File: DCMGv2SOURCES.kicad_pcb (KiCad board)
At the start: 2 copper layers, 232.7 x 74.2 mm, 170 parts, among them P10 NC_SCGR_SIG, P14 UNREG_V_SIG, P15 UNREG_I_SIG, P16 TO_REG+, P17 TO_REG-, P18 FROM_REG+, P19 FROM_REG-, P20 REG_V_SIG, P21 TO_GRID-, P22 REG_I_SIG, P23 TO_GRID+, P3 FROM_SRC+, P4 CTRL_SIG, P5 FROM_SRC-, P6 GND_IN, P7 IC+IN, P8 IC-IN, P9 COIL+IN, Q1 STS1DNC45, Q2 IRFP260, Q3 STS1DNC45, Q4 IRF5210, Q5 IRF5210, SW1 SPDT_RELAY, SW2 SPDT_RELAY, U1 LT1014DN, U10 LT1634, U11 LT1010, U12 LT1014DN, U13 LT1014DN, U14 ULN2803A, U2 LM339, U3 LT1634, U6 DAUGHTERBOARD_MOUNT, U7 LT1014DN, U8 LT1014DN, U9 LT1014DN

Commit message: added optional filtering capacitors for measurement amplifiers. corrected zener clamps to clamp high AND low voltages.
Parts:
- added C1: C, c_0603, B.Cu at (109.0, 71.4)
- added C10: C, c_0603, F.Cu at (136.9, 44.7)
- added C2: C, c_0603, F.Cu at (235.7, 78.2)
- added C3: C, c_0603, F.Cu at (77.2, 64.3)
- added C4: C, c_0603, F.Cu at (74.9, 69.1)
- added C5: C, c_0603, F.Cu at (154.9, 33.8)
- added C9: C, c_0603, F.Cu at (146.6, 43.9)
- added D15: BZX84C10L, SOT23, F.Cu at (131.6, 33.3)
- added D17: BZX84C10L, SOT23, F.Cu at (141.5, 36.3)
- added D18: BZX84C10L, SOT23, F.Cu at (164.3, 19.1)
- added D19: BZX84C10L, SOT23, F.Cu at (147.3, 31.8)
- moved D5 74.8 mm to (141.5, 32.5), turned to 90 degrees
- moved D4 65.8 mm to (133.9, 28.2), turned to 0 degrees
- moved D10 13.0 mm to (148.1, 35.3), turned to 270 degrees
- moved D7 9.35 mm to (160.5, 20.1), turned to 180 degrees
- moved R69 3.94 mm to (131.3, 43.7)
- moved R59 3.30 mm to (138.7, 41.7)
- moved R25 2.54 mm to (75.2, 64.3)
- moved R65 2.54 mm to (146.6, 45.7)
- moved R81 2.18 mm to (154.9, 29.2), turned to 270 degrees
- moved R79 2.03 mm to (143.0, 45.5)
- moved R58 0.92 mm to (136.1, 41.4)
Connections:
- D10 pad 1: CTRL_GND -> N-0000060
- D4 pad 1: CTRL_GND -> N-0000052
- D5 pad 1: CTRL_GND -> N-0000058
- D7 pad 1: CTRL_GND -> N-0000059
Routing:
- net CTRL_GND: track 192.2 -> 205.7 mm
- net N-0000096: track 226.9 -> 235.1 mm
- net N-0000031: track 13.7 -> 19.5 mm
- net N-0000055: track 5.20 -> 10.9 mm
- net N-0000091: track 62.2 -> 66.6 mm
- net N-0000052: track 0.00 -> 4.04 mm
- net N-0000053: track 8.75 -> 12.1 mm
- net N-0000030: track 95.7 -> 98.8 mm
- net N-0000059: track 0.00 -> 2.40 mm
- net N-0000051: track 5.97 -> 8.36 mm
- net N-0000065: track 8.92 -> 11.3 mm
- net N-0000054: track 14.8 -> 17.1 mm
- net N-0000060: track 0.00 -> 2.25 mm
- net N-0000049: track 16.5 -> 18.5 mm
- net N-0000098: track 30.7 -> 28.7 mm
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
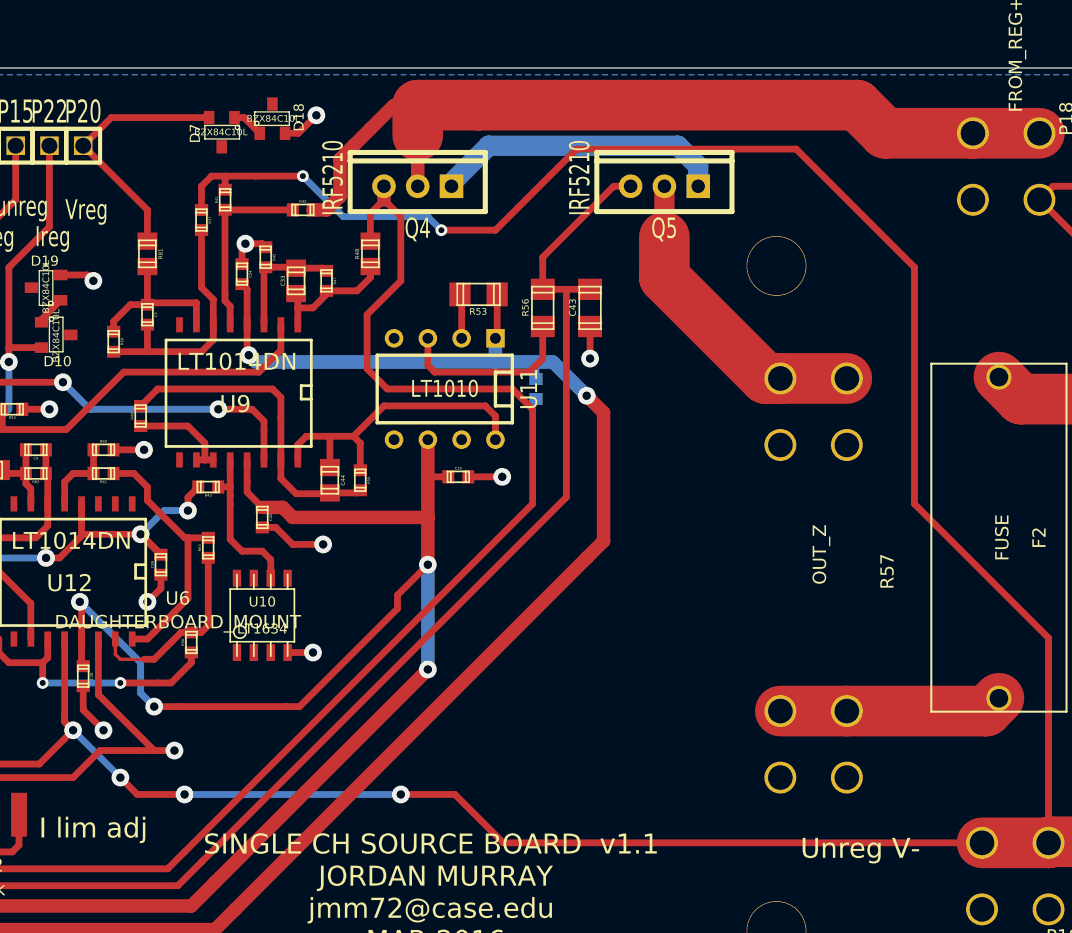
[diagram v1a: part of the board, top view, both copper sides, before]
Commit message: separated transistors for heat sink clearance
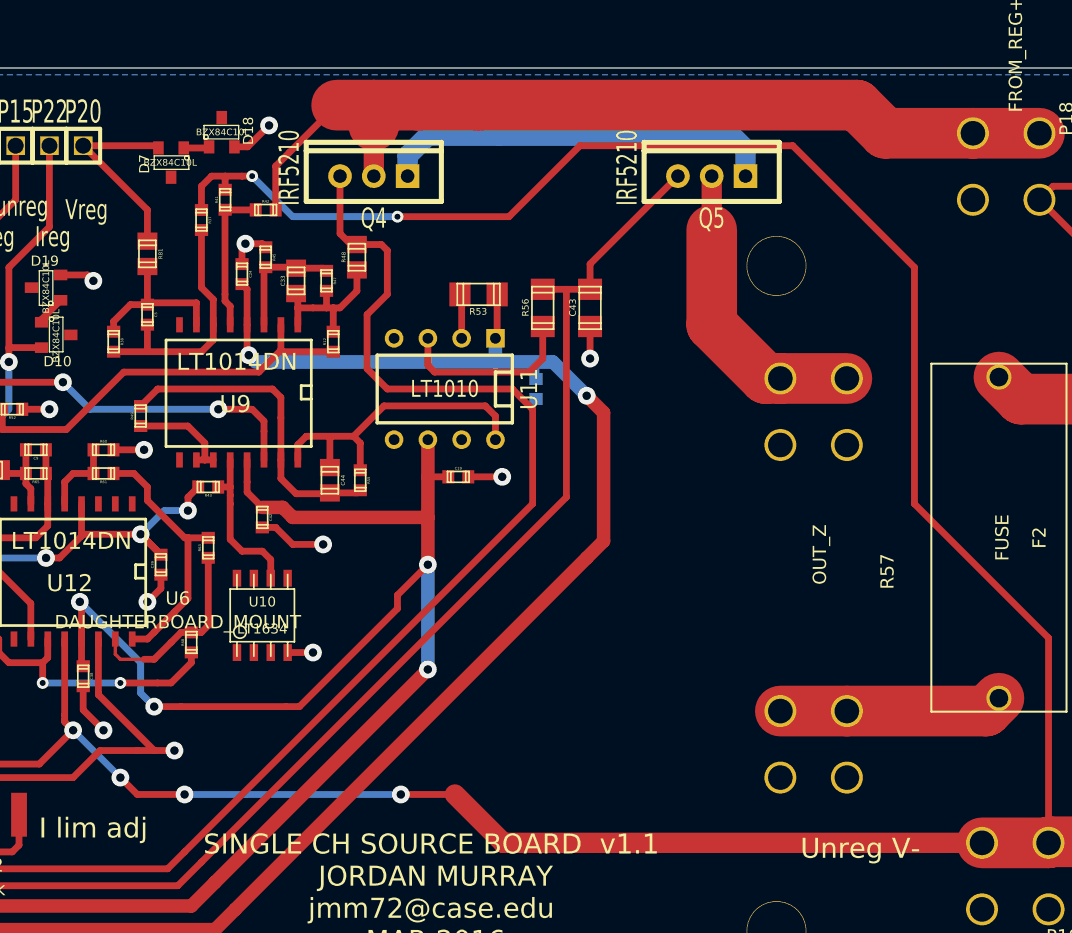
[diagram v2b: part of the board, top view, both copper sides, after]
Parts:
- added R12: 10M, c_0603, F.Cu at (168.9, 35.8)
- C1, C2: value C -> 10n
- C10, C3, C4, C5, C9: value C -> 2.2n
- moved D7 4.44 mm to (156.7, 22.4)
- moved D18 3.94 mm to (160.5, 20.1)
- moved Q5 3.64 mm to (197.4, 23.4)
- moved Q4 3.39 mm to (172.0, 23.4)
- moved R42 2.79 mm to (163.8, 25.9)
- moved R48 1.05 mm to (170.7, 29.5)
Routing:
- net N-0000058: track 22.1 -> 30.0 mm
- net N-0000033: track 19.5 -> 14.9 mm
- net N-0000049: track 80.7 -> 84.8 mm
- net N-0000042: track 28.6 -> 32.6 mm
- net N-0000045: track 13.9 -> 11.1 mm
- net N-0000029: track 9.79 -> 12.3 mm
- net N-0000030: track 193.1 -> 191.7 mm
- net N-0000057: track 23.7 -> 23.0 mm
- net N-0000096: track 235.1 -> 234.5 mm
- net CTRL_GND: track 205.7 -> 206.3 mm
